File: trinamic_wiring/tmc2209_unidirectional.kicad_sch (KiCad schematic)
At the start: 2 parts

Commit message: Make updates for new version of TMC2209 library
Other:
- company: (none) -> Janelia Research Campus
- title: (none) -> Trinamic Wiring
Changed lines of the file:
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@@
   (paper "A4")
   (title_block
+    (title "Trinamic Wiring")
     (date "2023-04-20")
+    (rev "0.3")
+    (company "Janelia Research Campus")
   )
   (no_connect (at 100.33 106.68))

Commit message: Redo schematic symbols
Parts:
- removed TMC?: TMC2209, symbol Janelia:SIMPLIFIED_TMC2209_UART
- removed microcontroller?: microcontroller, symbol Janelia:SIMPLIFIED_MCU_UART
- added MICROCONTROLLER4: DOC_MCU_UART, symbol Janelia:DOC_MCU_UART
- added TMC6: DOC_TMC2209, symbol Janelia:DOC_TMC2209
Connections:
- new net: MICROCONTROLLER4.1 (TX), TMC6.0 (UART)
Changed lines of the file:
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@@
     (company "Janelia Research Campus")
   )
-  (no_connect (at 100.33 106.68))
-  (wire (pts (xy 138.43 80.01) (xy 138.43 87.63))
+  (no_connect (at 119.38 105.41))
+  (wire (pts (xy 119.38 85.09) (xy 144.78 85.09))
     (stroke (width 0) (type default))
   )
-  (wire (pts (xy 100.33 87.63) (xy 138.43 87.63))
-    (stroke (width 0) (type default))
-  )
-  (symbol (lib_id "Janelia:SIMPLIFIED_MCU_UART") (at 87.63 96.52 0) (unit 1)
-    (in_bom yes) (on_board yes) (dnp no)
-    (property "Reference" "microcontroller?" (at 87.63 96.52 0) (do_not_autoplace)
+  (symbol (lib_id "Janelia:DOC_MCU_UART") (at 106.68 95.25 0) (unit 1)
+    (in_bom yes) (on_board yes) (dnp no) (fields_autoplaced)
+    (property "Reference" "MICROCONTROLLER4" (at 106.68 76.2 0) (do_not_autoplace)
+      (effects (font (size 1.27 1.27)) hide)
+    )
+    (property "Value" "DOC_MCU_UART" (at 106.68 81.28 0)
       (effects (font (size 1.524 1.524)) hide)
     )
-    (property "Value" "microcontroller" (at 87.63 96.52 0)
-      (effects (font (size 1.524 1.524)))
-    )
-    (property "Footprint" "" (at 85.09 123.19 0)
+    (property "Footprint" "" (at 104.14 121.92 0)
       (effects (font (size 1.524 1.524)) hide)
     )
-    (property "Datasheet" "" (at 87.63 96.52 0)
+    (property "Datasheet" "" (at 106.68 95.25 0)
       (effects (font (size 1.524 1.524)) hide)
+    )
+    (property "Sim.Enable" "0" (at 106.68 78.74 0)
+      (effects (font (size 1.27 1.27)) hide)
     )
     (pin "0")
@@
       (project "trinamic_wiring"
         (path "/e4144788-6304-493f-818e-5d881d3b7418/c8eda2b5-ab13-4033-82d9-875c9fcaf884/13e2a7b5-46df-44bb-8dde-5d79d190b8bf"
-          (reference "microcontroller?") (unit 1)
-        )
-        (path "/e4144788-6304-493f-818e-5d881d3b7418/c8eda2b5-ab13-4033-82d9-875c9fcaf884/e3613d8e-f506-47d6-ad2d-b0f5798d9847"
-          (reference "microcontroller1") (unit 1)
-        )
-        (path "/e4144788-6304-493f-818e-5d881d3b7418/c8eda2b5-ab13-4033-82d9-875c9fcaf884/5b0a2695-6b0b-4c82-b9d6-7e19fee75501"
-          (reference "microcontroller3") (unit 1)
+          (reference "MICROCONTROLLER4") (unit 1)
         )
       )
     )
   )
-  (symbol (lib_id "Janelia:SIMPLIFIED_TMC2209_UART") (at 138.43 64.77 0) (unit 1)
+  (symbol (lib_id "Janelia:DOC_TMC2209") (at 157.48 95.25 0) (unit 1)
     (in_bom yes) (on_board yes) (dnp no) (fields_autoplaced)
-    (property "Reference" "TMC?" (at 138.43 64.77 0) (do_not_autoplace)
+    (property "Reference" "TMC6" (at 157.48 76.2 0)
+      (effects (font (size 1.27 1.27)) hide)
+    )
+    (property "Value" "DOC_TMC2209" (at 157.48 81.28 0)
       (effects (font (size 1.524 1.524)) hide)
     )
-    (property "Value" "TMC2209" (at 138.43 64.77 0)
-      (effects (font (size 1.524 1.524)))
-    )
-    (property "Footprint" "" (at 135.89 91.44 0)
+    (property "Footprint" "" (at 154.94 121.92 0)
       (effects (font (size 1.524 1.524)) hide)
     )
-    (property "Datasheet" "" (at 138.43 64.77 0)
+    (property "Datasheet" "" (at 157.48 95.25 0)
       (effects (font (size 1.524 1.524)) hide)
     )
+    (property "Sim.Enable" "0" (at 157.48 78.74 0)
+      (effects (font (size 1.27 1.27)) hide)
+    )
     (pin "0")
+    (pin "1")
+    (pin "10")
+    (pin "2")
+    (pin "3")
+    (pin "4")
+    (pin "5")
+    (pin "6")
+    (pin "7")
+    (pin "8")
+    (pin "9")
     (instances
       (project "trinamic_wiring"
         (path "/e4144788-6304-493f-818e-5d881d3b7418/c8eda2b5-ab13-4033-82d9-875c9fcaf884/13e2a7b5-46df-44bb-8dde-5d79d190b8bf"
-          (reference "TMC?") (unit 1)
-        )
-        (path "/e4144788-6304-493f-818e-5d881d3b7418/c8eda2b5-ab13-4033-82d9-875c9fcaf884/e3613d8e-f506-47d6-ad2d-b0f5798d9847"
-          (reference "TMC1") (unit 1)
-        )
-        (path "/e4144788-6304-493f-818e-5d881d3b7418/c8eda2b5-ab13-4033-82d9-875c9fcaf884/5b0a2695-6b0b-4c82-b9d6-7e19fee75501"
-          (reference "TMC4") (unit 1)
+          (reference "TMC6") (unit 1)
         )
       )

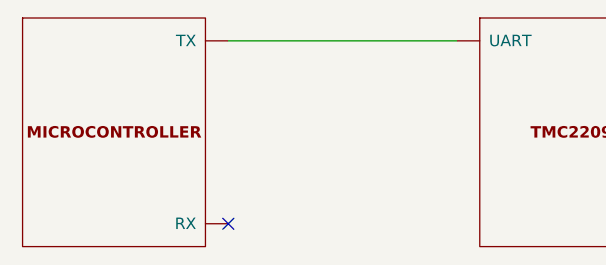
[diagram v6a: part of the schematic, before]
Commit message: Add more schematics
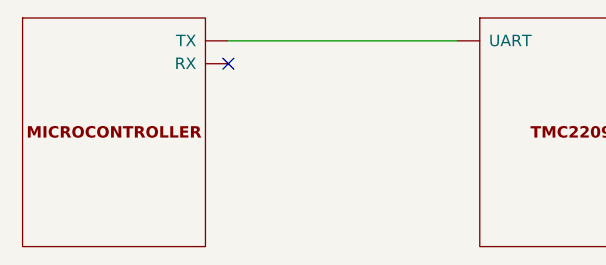
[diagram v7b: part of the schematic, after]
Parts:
- removed MICROCONTROLLER4: DOC_MCU_UART, symbol Janelia:DOC_MCU_UART
- added MICROCONTROLLER4: DOC_MCU, symbol Janelia:DOC_MCU
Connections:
- net at TMC6.0 (UART): now also MICROCONTROLLER4.1 (TX)
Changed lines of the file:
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@@
   (title_block
     (title "Trinamic Wiring")
-    (date "2023-08-01")
+    (date "2023-08-02")
     (rev "0.4")
     (company "Janelia Research Campus")
   )
-  (no_connect (at 119.38 105.41))
+  (no_connect (at 119.38 87.63))
   (wire (pts (xy 119.38 85.09) (xy 144.78 85.09))
     (stroke (width 0) (type default))
   )
-  (symbol (lib_id "Janelia:DOC_MCU_UART") (at 106.68 95.25 0) (unit 1)
+  (symbol (lib_id "Janelia:DOC_MCU") (at 106.68 95.25 0) (unit 1)
     (in_bom yes) (on_board yes) (dnp no) (fields_autoplaced)
-    (property "Reference" "MICROCONTROLLER4" (at 106.68 76.2 0) (do_not_autoplace)
+    (property "Reference" "MICROCONTROLLER4" (at 106.68 76.2 0)
       (effects (font (size 1.27 1.27)) hide)
     )
-    (property "Value" "DOC_MCU_UART" (at 106.68 81.28 0)
+    (property "Value" "DOC_MCU" (at 106.68 81.28 0)
       (effects (font (size 1.524 1.524)) hide)
     )
@@
     (pin "0")
     (pin "1")
+    (pin "2")
+    (pin "3")
+    (pin "4")
+    (pin "5")
+    (pin "6")
+    (pin "7")
+    (pin "8")
     (instances
       (project "trinamic_wiring"
         (path "/e4144788-6304-493f-818e-5d881d3b7418/c8eda2b5-ab13-4033-82d9-875c9fcaf884/13e2a7b5-46df-44bb-8dde-5d79d190b8bf"
           (reference "MICROCONTROLLER4") (unit 1)
+        )
+        (path "/e4144788-6304-493f-818e-5d881d3b7418/c8eda2b5-ab13-4033-82d9-875c9fcaf884/8277c47e-3fcc-48ef-9892-6d34b4c51a79"
+          (reference "MICROCONTROLLER8") (unit 1)
         )
       )
@@
           (reference "TMC6") (unit 1)
         )
+        (path "/e4144788-6304-493f-818e-5d881d3b7418/c8eda2b5-ab13-4033-82d9-875c9fcaf884/8277c47e-3fcc-48ef-9892-6d34b4c51a79"
+          (reference "TMC13") (unit 1)
+        )
       )
